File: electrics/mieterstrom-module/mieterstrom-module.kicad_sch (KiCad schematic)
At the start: 25 parts, among them J1 North, J2 South, J3 West, J4 East, U1 BA033CC0FP-E2, U2 MAX3486, U3 MAX3486

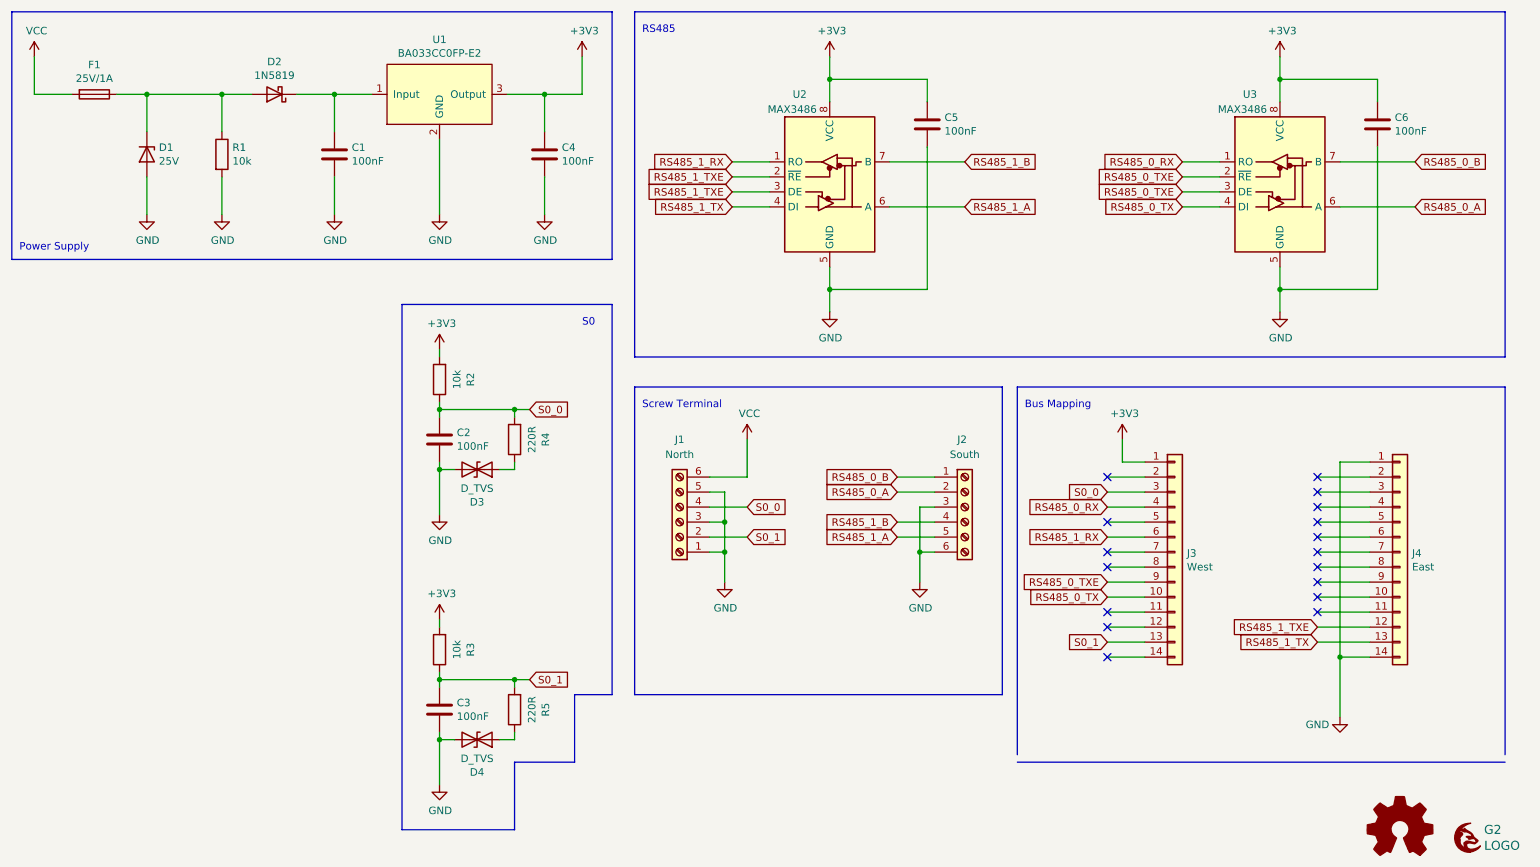
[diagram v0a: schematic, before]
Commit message: Fix all ERC and DRC warnings during build
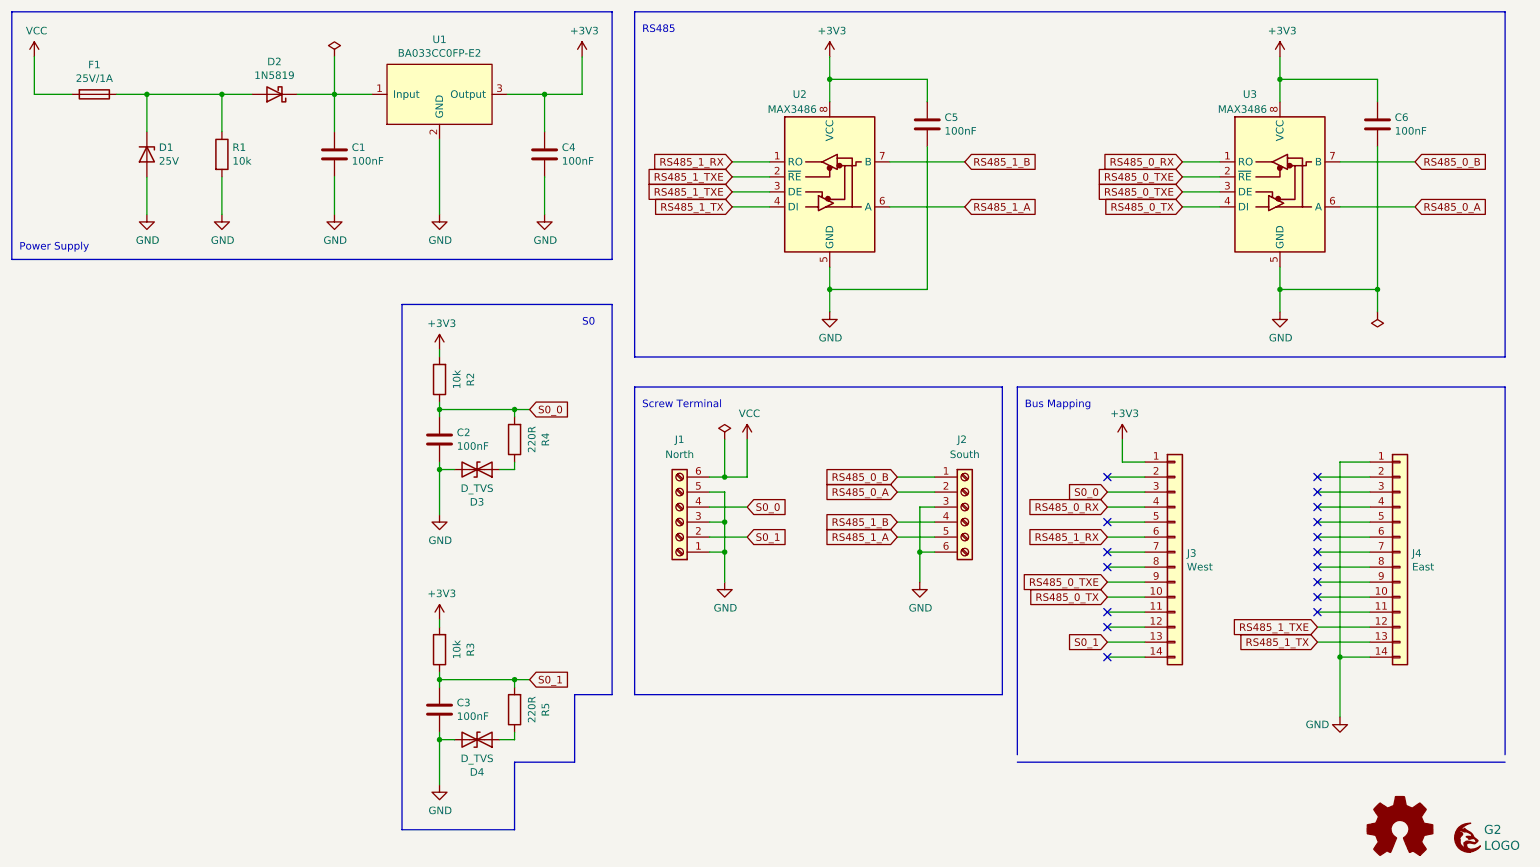
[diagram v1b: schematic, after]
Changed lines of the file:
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@@
   (junction (at 74.93 33.02) (diameter 0) (color 0 0 0 0)
   )
+  (junction (at 251.46 66.04) (diameter 0) (color 0 0 0 0)
+  )
   (junction (at 92.71 96.52) (diameter 0) (color 0 0 0 0)
   )
   (junction (at 158.75 30.48) (diameter 0) (color 0 0 0 0)
+  )
+  (junction (at 140.97 97.79) (diameter 0) (color 0 0 0 0)
   )
   (junction (at 234.95 30.48) (diameter 0) (color 0 0 0 0)
@@
     (stroke (width 0) (type default) (color 0 0 0 0))
   )
+  (wire (pts (xy 140.97 97.79) (xy 144.78 97.79))
+    (stroke (width 0) (type default) (color 0 0 0 0))
+  )
   (polyline (pts (xy 273.05 19.05) (xy 273.05 77.47))
     (stroke (width 0) (type default) (color 0 0 0 0))
@@
     (stroke (width 0) (type default) (color 0 0 0 0))
   )
+  (wire (pts (xy 140.97 91.44) (xy 140.97 97.79))
+    (stroke (width 0) (type default) (color 0 0 0 0))
+  )
   (wire (pts (xy 234.95 30.48) (xy 234.95 34.29))
     (stroke (width 0) (type default) (color 0 0 0 0))
@@
     (stroke (width 0) (type default) (color 0 0 0 0))
   )
-  (wire (pts (xy 138.43 97.79) (xy 144.78 97.79))
+  (wire (pts (xy 138.43 97.79) (xy 140.97 97.79))
     (stroke (width 0) (type default) (color 0 0 0 0))
   )
@@
   )
   (wire (pts (xy 102.87 142.24) (xy 105.41 142.24))
+    (stroke (width 0) (type default) (color 0 0 0 0))
+  )
+  (wire (pts (xy 74.93 26.67) (xy 74.93 33.02))
+    (stroke (width 0) (type default) (color 0 0 0 0))
+  )
+  (wire (pts (xy 251.46 66.04) (xy 251.46 69.85))
     (stroke (width 0) (type default) (color 0 0 0 0))
   )
@@
     (pin "2")
   )
+  (symbol (lib_id "power:PWR_FLAG") (at 251.46 69.85 180) (unit 1)
+    (in_bom yes) (on_board yes) (fields_autoplaced)
+    (property "Reference" "#FLG0101" (id 0) (at 251.46 71.755 0)
+      (effects (font (size 1.27 1.27)) hide)
+    )
+    (property "Value" "PWR_FLAG" (id 1) (at 251.46 74.93 0)
+      (effects (font (size 1.27 1.27)) hide)
+    )
+    (property "Footprint" "" (id 2) (at 251.46 69.85 0)
+      (effects (font (size 1.27 1.27)) hide)
+    )
+    (property "Datasheet" "~" (id 3) (at 251.46 69.85 0)
+      (effects (font (size 1.27 1.27)) hide)
+    )
+    (pin "1")
+  )
   (symbol (lib_id "power:GND") (at 173.99 115.57 0) (unit 1)
     (in_bom yes) (on_board yes)
@@
     (pin "2")
   )
+  (symbol (lib_id "power:PWR_FLAG") (at 140.97 91.44 0) (unit 1)
+    (in_bom yes) (on_board yes) (fields_autoplaced)
+    (property "Reference" "#FLG0103" (id 0) (at 140.97 89.535 0)
+      (effects (font (size 1.27 1.27)) hide)
+    )
+    (property "Value" "PWR_FLAG" (id 1) (at 140.97 86.36 0)
+      (effects (font (size 1.27 1.27)) hide)
+    )
+    (property "Footprint" "" (id 2) (at 140.97 91.44 0)
+      (effects (font (size 1.27 1.27)) hide)
+    )
+    (property "Datasheet" "~" (id 3) (at 140.97 91.44 0)
+      (effects (font (size 1.27 1.27)) hide)
+    )
+    (pin "1")
+  )
   (symbol (lib_id "Device:C") (at 251.46 38.1 0) (unit 1)
     (in_bom yes) (on_board yes)
@@
     (pin "1")
     (pin "2")
+  )
+  (symbol (lib_id "power:PWR_FLAG") (at 74.93 26.67 0) (unit 1)
+    (in_bom yes) (on_board yes) (fields_autoplaced)
+    (property "Reference" "#FLG0104" (id 0) (at 74.93 24.765 0)
+      (effects (font (size 1.27 1.27)) hide)
+    )
+    (property "Value" "PWR_FLAG" (id 1) (at 74.93 21.59 0)
+      (effects (font (size 1.27 1.27)) hide)
+    )
+    (property "Footprint" "" (id 2) (at 74.93 26.67 0)
+      (effects (font (size 1.27 1.27)) hide)
+    )
+    (property "Datasheet" "~" (id 3) (at 74.93 26.67 0)
+      (effects (font (size 1.27 1.27)) hide)
+    )
+    (pin "1")
   )
   (symbol (lib_id "Interface_UART:MAX3486") (at 158.75 46.99 0) (unit 1)
@@
   )
   (symbol_instances
+    (path "/6044eb93-ce75-4800-a2c5-fc714976775e"
+      (reference "#FLG0101") (unit 1) (value "PWR_FLAG") (footprint "")
+    )
+    (path "/6ec8c0d7-5dd8-49a5-9ac1-e5b4733e56d6"
+      (reference "#FLG0103") (unit 1) (value "PWR_FLAG") (footprint "")
+    )
+    (path "/b3b99b81-0687-4be3-8a61-f98233710b65"
+      (reference "#FLG0104") (unit 1) (value "PWR_FLAG") (footprint "")
+    )
     (path "/a067890f-6be8-49e9-b75d-ff2c32452685"
       (reference "#PWR0101") (unit 1) (value "GND") (footprint "")
